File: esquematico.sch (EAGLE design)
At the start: 5 parts, among them U1 ROB-14450

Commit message: Create DRV8833 Lib
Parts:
- added U$2: DRV8833, DRV8833:DRV8833
- added X2, X3: (no value), con-ptr500:AK300/2
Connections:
- new net N$1: X2-1.KL
- new net N$3: X2-2.KL
- new net N$4: X3-1.KL
- new net N$5: X3-2.KL
- net BL: now also U$1.PA15
- net CE: now also U$1.PB7; no longer U$1.PB6
- net CLK: now also U$1.PB3; no longer U$1.PB9
- net DC: now also U$1.PB6; no longer U$1.PB7
- net DIN: now also U$1.PB5; no longer U$1.PB8
- net RST: now also U$1.PB8; no longer U$1.PB5
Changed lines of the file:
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@@
 <part name="DISPLAY" library="pinhead" library_urn="urn:adsk.eagle:library:325" deviceset="PINHD-1X8" device="" package3d_urn="urn:adsk.eagle:package:22409/2"/>
 <part name="X1" library="con-ptr500" library_urn="urn:adsk.eagle:library:181" deviceset="AK300/2" device="" package3d_urn="urn:adsk.eagle:package:9881/1"/>
+<part name="X2" library="con-ptr500" library_urn="urn:adsk.eagle:library:181" deviceset="AK300/2" device="" package3d_urn="urn:adsk.eagle:package:9881/1"/>
+<part name="X3" library="con-ptr500" library_urn="urn:adsk.eagle:library:181" deviceset="AK300/2" device="" package3d_urn="urn:adsk.eagle:package:9881/1"/>
+<part name="U$2" library="DRV8833" deviceset="DRV8833" device=""/>
 </parts>
 <sheets>
@@
 <attribute name="VALUE" x="-643.89" y="550.037" size="1.778" layer="96"/>
 </instance>
+<instance part="X2" gate="-1" x="-508" y="619.76" smashed="yes" rot="MR0">
+<attribute name="NAME" x="-506.73" y="620.649" size="1.778" layer="95" rot="MR180"/>
+</instance>
+<instance part="X2" gate="-2" x="-508" y="614.68" smashed="yes" rot="MR0">
+<attribute name="NAME" x="-506.73" y="615.569" size="1.778" layer="95" rot="MR180"/>
+<attribute name="VALUE" x="-504.19" y="610.997" size="1.778" layer="96" rot="MR0"/>
+</instance>
+<instance part="X3" gate="-1" x="-508" y="607.06" smashed="yes" rot="MR0">
+<attribute name="NAME" x="-506.73" y="607.949" size="1.778" layer="95" rot="MR180"/>
+</instance>
+<instance part="X3" gate="-2" x="-508" y="601.98" smashed="yes" rot="MR0">
+<attribute name="NAME" x="-506.73" y="602.869" size="1.778" layer="95" rot="MR180"/>
+<attribute name="VALUE" x="-504.19" y="598.297" size="1.778" layer="96" rot="MR0"/>
+</instance>
+<instance part="U$2" gate="G$1" x="-505.46" y="556.26" smashed="yes">
+<attribute name="VALUE" x="-515.62" y="558.8" size="1.778" layer="94"/>
+</instance>
 </instances>
 <busses>
@@
 </segment>
 <segment>
+<pinref part="U$1" gate="G$1" pin="PB8"/>
+<wire x1="-640.08" y1="581.66" x2="-645.16" y2="581.66" width="0.1524" layer="91"/>
+<label x="-645.16" y="581.66" size="1.016" layer="95" rot="R180" xref="yes"/>
+</segment>
+</net>
+<net name="CE" class="0">
+<segment>
+<pinref part="DISPLAY" gate="A" pin="2"/>
+<wire x1="-581.66" y1="579.12" x2="-574.04" y2="579.12" width="0.1524" layer="91"/>
+<label x="-574.04" y="579.12" size="1.016" layer="95" xref="yes"/>
+</segment>
+<segment>
+<pinref part="U$1" gate="G$1" pin="PB7"/>
+<wire x1="-640.08" y1="584.2" x2="-645.16" y2="584.2" width="0.1524" layer="91"/>
+<label x="-645.16" y="584.2" size="1.016" layer="95" rot="R180" xref="yes"/>
+</segment>
+</net>
+<net name="DC" class="0">
+<segment>
+<pinref part="DISPLAY" gate="A" pin="3"/>
+<wire x1="-581.66" y1="576.58" x2="-574.04" y2="576.58" width="0.1524" layer="91"/>
+<label x="-574.04" y="576.58" size="1.016" layer="95" xref="yes"/>
+</segment>
+<segment>
+<pinref part="U$1" gate="G$1" pin="PB6"/>
+<wire x1="-640.08" y1="586.74" x2="-645.16" y2="586.74" width="0.1524" layer="91"/>
+<label x="-645.16" y="586.74" size="1.016" layer="95" rot="R180" xref="yes"/>
+</segment>
+</net>
+<net name="DIN" class="0">
+<segment>
+<pinref part="DISPLAY" gate="A" pin="4"/>
+<wire x1="-581.66" y1="574.04" x2="-574.04" y2="574.04" width="0.1524" layer="91"/>
+<label x="-574.04" y="574.04" size="1.016" layer="95" xref="yes"/>
+</segment>
+<segment>
 <pinref part="U$1" gate="G$1" pin="PB5"/>
 <wire x1="-640.08" y1="589.28" x2="-645.16" y2="589.28" width="0.1524" layer="91"/>
@@
 </segment>
 </net>
-<net name="CE" class="0">
-<segment>
-<pinref part="DISPLAY" gate="A" pin="2"/>
-<wire x1="-581.66" y1="579.12" x2="-574.04" y2="579.12" width="0.1524" layer="91"/>
-<label x="-574.04" y="579.12" size="1.016" layer="95" xref="yes"/>
-</segment>
-<segment>
-<pinref part="U$1" gate="G$1" pin="PB6"/>
-<wire x1="-640.08" y1="586.74" x2="-645.16" y2="586.74" width="0.1524" layer="91"/>
-<label x="-645.16" y="586.74" size="1.016" layer="95" rot="R180" xref="yes"/>
-</segment>
-</net>
-<net name="DC" class="0">
-<segment>
-<pinref part="DISPLAY" gate="A" pin="3"/>
-<wire x1="-581.66" y1="576.58" x2="-574.04" y2="576.58" width="0.1524" layer="91"/>
-<label x="-574.04" y="576.58" size="1.016" layer="95" xref="yes"/>
-</segment>
-<segment>
-<pinref part="U$1" gate="G$1" pin="PB7"/>
-<wire x1="-640.08" y1="584.2" x2="-645.16" y2="584.2" width="0.1524" layer="91"/>
-<label x="-645.16" y="584.2" size="1.016" layer="95" rot="R180" xref="yes"/>
-</segment>
-</net>
-<net name="DIN" class="0">
-<segment>
-<pinref part="DISPLAY" gate="A" pin="4"/>
-<wire x1="-581.66" y1="574.04" x2="-574.04" y2="574.04" width="0.1524" layer="91"/>
-<label x="-574.04" y="574.04" size="1.016" layer="95" xref="yes"/>
-</segment>
-<segment>
-<pinref part="U$1" gate="G$1" pin="PB8"/>
-<wire x1="-640.08" y1="581.66" x2="-645.16" y2="581.66" width="0.1524" layer="91"/>
-<label x="-645.16" y="581.66" size="1.016" layer="95" rot="R180" xref="yes"/>
-</segment>
-</net>
 <net name="CLK" class="0">
 <segment>
@@
 </segment>
 <segment>
-<pinref part="U$1" gate="G$1" pin="PB9"/>
-<wire x1="-640.08" y1="579.12" x2="-645.16" y2="579.12" width="0.1524" layer="91"/>
-<label x="-645.16" y="579.12" size="1.016" layer="95" rot="R180" xref="yes"/>
+<pinref part="U$1" gate="G$1" pin="PB3"/>
+<wire x1="-640.08" y1="594.36" x2="-645.16" y2="594.36" width="0.1524" layer="91"/>
+<label x="-645.16" y="594.36" size="1.016" layer="95" rot="R180" xref="yes"/>
 </segment>
 </net>
@@
 <label x="-574.04" y="566.42" size="1.016" layer="95" xref="yes"/>
 </segment>
-</net>
-<net name="N$6" class="0">
-<segment>
-<pinref part="U$1" gate="G$1" pin="PB4"/>
-<wire x1="-640.08" y1="591.82" x2="-645.16" y2="591.82" width="0.1524" layer="91"/>
+<segment>
+<pinref part="U$1" gate="G$1" pin="PA15"/>
+<wire x1="-640.08" y1="596.9" x2="-645.16" y2="596.9" width="0.1524" layer="91"/>
+<label x="-645.16" y="596.9" size="1.016" layer="95" rot="R180" xref="yes"/>
 </segment>
 </net>
@@
 </segment>
 </net>
+<net name="N$2" class="0">
+<segment>
+<pinref part="U$1" gate="G$1" pin="PB4"/>
+<wire x1="-640.08" y1="591.82" x2="-645.16" y2="591.82" width="0.1524" layer="91"/>
+</segment>
+</net>
+<net name="N$1" class="0">
+<segment>
+<pinref part="X2" gate="-1" pin="KL"/>
+<wire x1="-513.08" y1="619.76" x2="-515.62" y2="619.76" width="0.1524" layer="91"/>
+</segment>
+</net>
+<net name="N$3" class="0">
+<segment>
+<pinref part="X2" gate="-2" pin="KL"/>
+<wire x1="-513.08" y1="614.68" x2="-515.62" y2="614.68" width="0.1524" layer="91"/>
+</segment>
+</net>
+<net name="N$4" class="0">
+<segment>
+<pinref part="X3" gate="-1" pin="KL"/>
+<wire x1="-513.08" y1="607.06" x2="-515.62" y2="607.06" width="0.1524" layer="91"/>
+</segment>
+</net>
+<net name="N$5" class="0">
+<segment>
+<pinref part="X3" gate="-2" pin="KL"/>
+<wire x1="-513.08" y1="601.98" x2="-515.62" y2="601.98" width="0.1524" layer="91"/>
+</segment>
+</net>

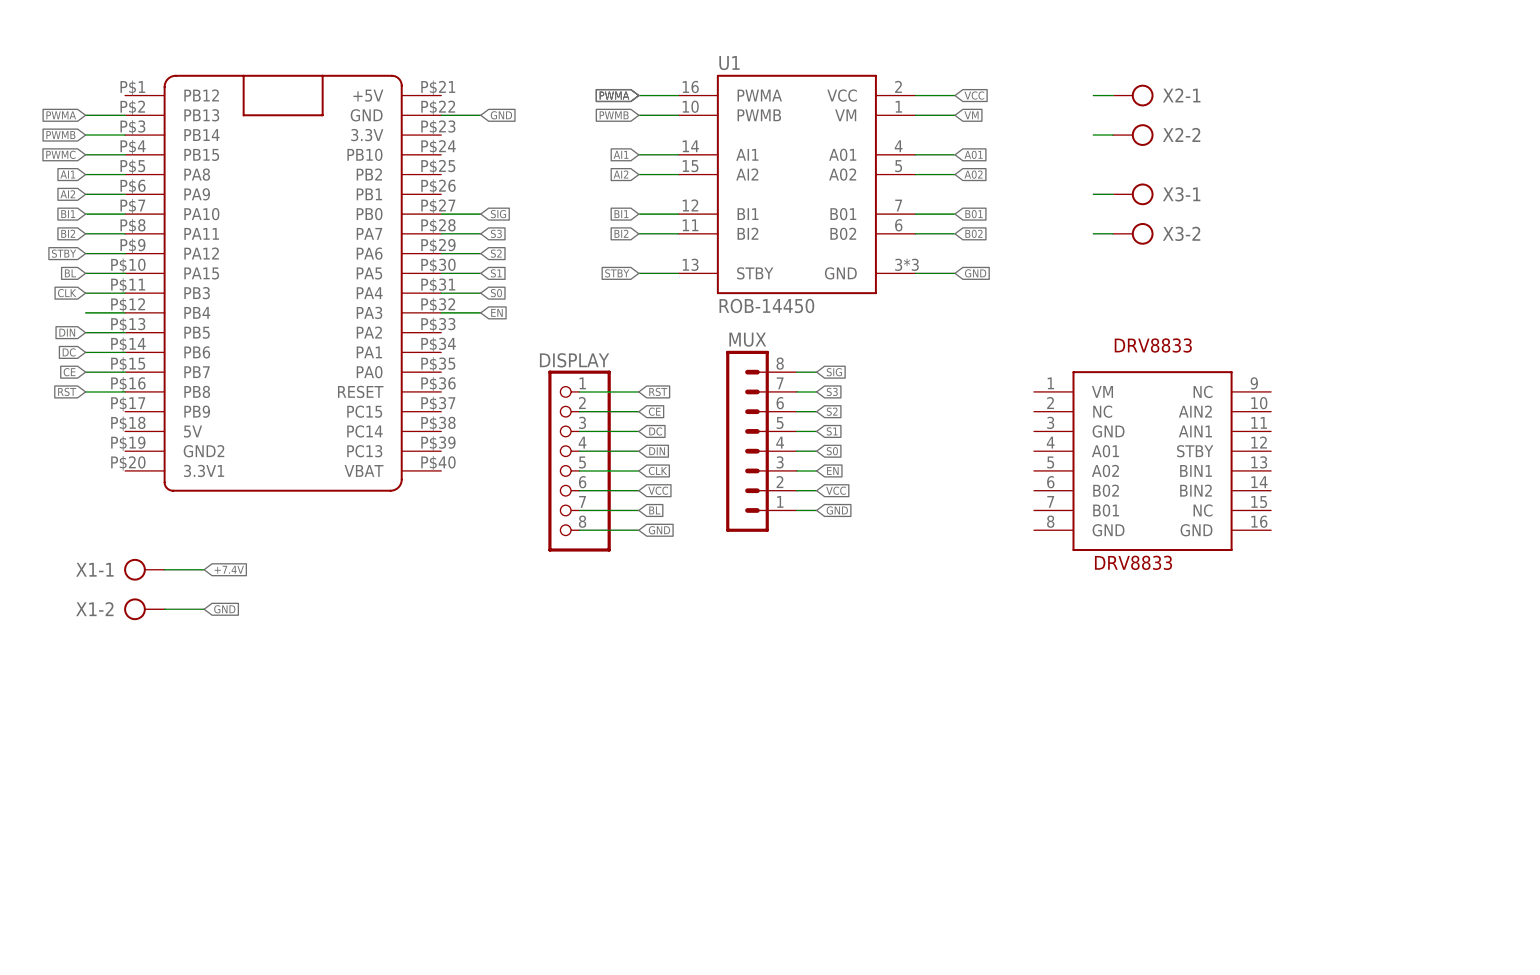
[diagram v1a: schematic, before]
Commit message: Atualização Pinos STM32 e Lib
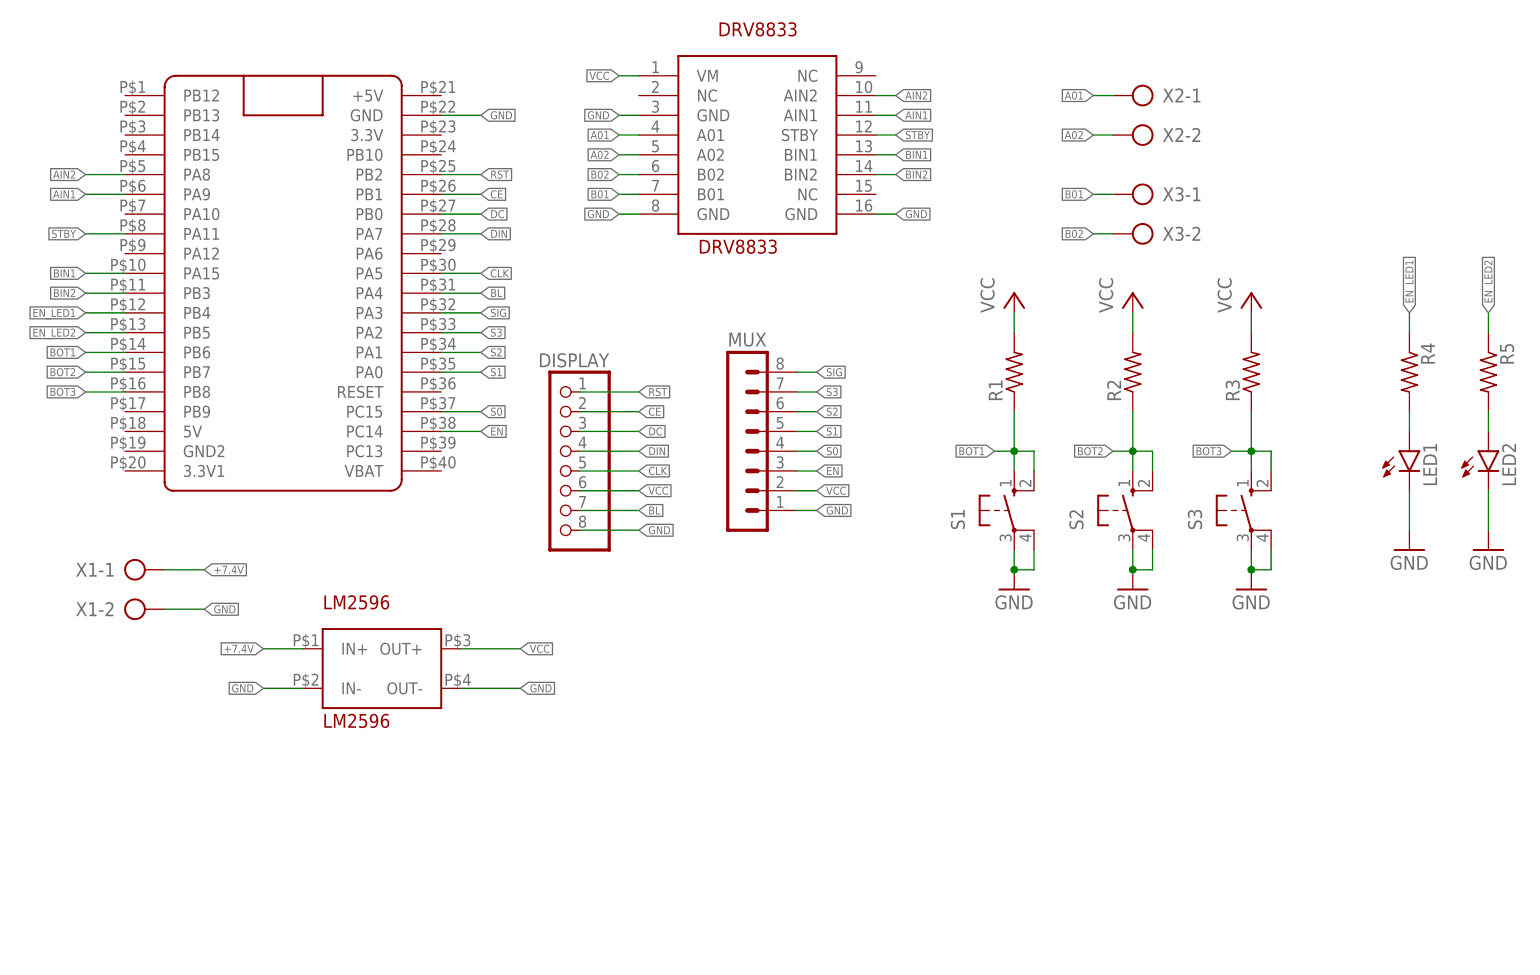
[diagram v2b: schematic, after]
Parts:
- removed U1: ROB-14450, ROB-14450:ROB-14450
- added LED1, LED2: (no value), led:LED5MM
- added R1, R2, R3, R4, R5: (no value), rcl:R-US_0204/5
- added S1, S2, S3: (no value), switch-omron:10-XX
- added U$3: LM2596, DRV8833:LM2596
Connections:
- removed net AI1: U$1.PA8, U1.AI1
- removed net AI2: U$1.PA9, U1.AI2
- removed net BI1: U$1.PA10, U1.BI1
- removed net BI2: U$1.PA11, U1.BI2
- removed net N$3: X2-2.KL
- removed net N$4: X3-1.KL
- removed net N$5: X3-2.KL
- removed net PWMA: U$1.PB13, U1.PWMA
- removed net PWMB: U$1.PB14, U1.PWMB
- removed net PWMC: U$1.PB15
- removed net VM: U1.VM
- new net AIN1: U$1.PA9, U$2.AIN1
- new net AIN2: U$1.PA8, U$2.AIN2
- new net BIN1: U$1.PA15, U$2.BIN1
- new net BIN2: U$1.PB3, U$2.BIN2
- new net BOT1: R1.1, S1.S, S1.S1, U$1.PB6
- new net BOT2: R2.1, S2.S, S2.S1, U$1.PB7
- new net BOT3: R3.1, S3.S, S3.S1, U$1.PB8
- new net EN_LED1: R4.1, U$1.PB4
- new net EN_LED2: R5.1, U$1.PB5
- net +7.4V: now also U$3.IN+
- net A01: now also U$2.A01, X2-1.KL; no longer U1.A01
- net A02: now also U$2.A02, X2-2.KL; no longer U1.A02
- net B01: now also U$2.B01, X3-1.KL; no longer U1.B01
- net B02: now also U$2.B02, X3-2.KL; no longer U1.B02
- net BL: now also U$1.PA4; no longer U$1.PA15
- net CE: now also U$1.PB1; no longer U$1.PB7
- net CLK: now also U$1.PA5; no longer U$1.PB3
- net DC: now also U$1.PB0; no longer U$1.PB6
- net DIN: now also U$1.PA7; no longer U$1.PB5
- net EN: now also U$1.PC14; no longer U$1.PA3
- net GND: now also LED1.C, LED2.C, S1.P, S1.P1, S2.P, S2.P1, S3.P, S3.P1, U$2.GND@1, U$2.GND@2, U$2.GND@3, U$3.IN-, U$3.OUT-; no longer U1.GND
- net N$1: now also LED1.A, R4.2; no longer X2-1.KL
- net N$2: now also LED2.A, R5.2; no longer U$1.PB4
- net RST: now also U$1.PB2; no longer U$1.PB8
- net S0: now also U$1.PC15; no longer U$1.PA4
- net S1: now also U$1.PA0; no longer U$1.PA5
- net S2: now also U$1.PA1; no longer U$1.PA6
- net S3: now also U$1.PA2; no longer U$1.PA7
- net SIG: now also U$1.PA3; no longer U$1.PB0
- net STBY: now also U$1.PA11, U$2.STBY; no longer U$1.PA12, U1.STBY
- net VCC: now also R1.2, R2.2, R3.2, U$2.VM, U$3.OUT+; no longer U1.VCC

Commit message: Atualização Drive
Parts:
- removed U$2: DRV8833, DRV8833:DRV8833
- added U1: ROB-14450, ROB-14450:ROB-14450
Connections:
- removed net AIN1: U$1.PA9, U$2.AIN1
- removed net AIN2: U$1.PA8, U$2.AIN2
- removed net BIN1: U$1.PA15, U$2.BIN1
- removed net BIN2: U$1.PB3, U$2.BIN2
- new net AI1: U$1.PA10, U1.AI1
- new net AI2: U$1.PA9, U1.AI2
- new net BI1: U$1.PA12, U1.BI1
- new net BI2: U$1.PA15, U1.BI2
- new net PWMA: U$1.PA8, U1.PWMA
- new net PWMB: U$1.PB3, U1.PWMB
- net A01: now also U1.A01; no longer U$2.A01
- net A02: now also U1.A02; no longer U$2.A02
- net B01: now also U1.B01; no longer U$2.B01
- net B02: now also U1.B02; no longer U$2.B02
- net GND: now also U1.GND; no longer U$2.GND@1, U$2.GND@2, U$2.GND@3
- net STBY: now also U1.STBY; no longer U$2.STBY
- net VCC: now also U1.VCC, U1.VM; no longer U$2.VM

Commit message: Att Lib
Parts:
- removed DISPLAY: (no value), pinhead:PINHD-1X8
- added U$2: NOKIA5110, DRV8833:NOKIA5110
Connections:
- net BL: now also U$2.7; no longer DISPLAY.7
- net CE: now also U$2.2; no longer DISPLAY.2
- net CLK: now also U$2.5; no longer DISPLAY.5
- net DC: now also U$2.3; no longer DISPLAY.3
- net DIN: now also U$2.4; no longer DISPLAY.4
- net GND: now also U$2.8; no longer DISPLAY.8
- net RST: now also U$2.1; no longer DISPLAY.1
- net VCC: now also U$1.3.3V, U$2.6; no longer DISPLAY.6

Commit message: Trilhas V1
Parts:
- removed LED1, LED2: (no value), led:LED5MM
- removed R3, R4, R5: (no value), rcl:R-US_0204/5
- removed S3: (no value), switch-omron:10-XX
- R1, R2: device rcl:R-US_0204/5 -> rcl:R-US_0204/7
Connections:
- removed net BOT3: R3.1, S3.S, S3.S1, U$1.PB8
- removed net EN_LED1: R4.1, U$1.PB4
- removed net EN_LED2: R5.1, U$1.PB5
- removed net N$1: LED1.A, R4.2
- removed net N$2: LED2.A, R5.2
- net BOT1: now also U$1.PB9; no longer U$1.PB6
- net BOT2: now also U$1.PB8; no longer U$1.PB7
- net GND: no longer LED1.C, LED2.C, S3.P, S3.P1
- net VCC: no longer R3.2

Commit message: Trilhas V3
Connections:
- net VCC: now also U$1.+5V; no longer U$1.3.3V
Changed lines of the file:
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@@
 </segment>
 <segment>
-<pinref part="U$1" gate="G$1" pin="3.3V"/>
-<wire x1="-599.44" y1="614.68" x2="-594.36" y2="614.68" width="0.1524" layer="91"/>
-<label x="-594.36" y="614.68" size="1.016" layer="95" xref="yes"/>
+<pinref part="U$1" gate="G$1" pin="+5V"/>
+<wire x1="-599.44" y1="619.76" x2="-594.36" y2="619.76" width="0.1524" layer="91"/>
+<label x="-594.36" y="619.76" size="1.016" layer="95" xref="yes"/>
 </segment>
 </net>

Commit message: Trilhas V4
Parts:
- removed MUX: (no value), con-lstb:MA08-1
- added SV1: (no value), con-amp-mt:S08P
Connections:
- net EN: now also SV1-6.S; no longer MUX.3
- net GND: now also SV1-8.S; no longer MUX.1
- net S0: now also SV1-5.S; no longer MUX.4
- net S1: now also SV1-4.S; no longer MUX.5
- net S2: now also SV1-3.S; no longer MUX.6
- net S3: now also SV1-2.S; no longer MUX.7
- net SIG: now also SV1-1.S; no longer MUX.8
- net VCC: now also SV1-7.S; no longer MUX.2
